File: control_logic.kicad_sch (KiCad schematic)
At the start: 33 parts, among them J18 USB_A_Stacked, J19 USB, J20 CTRL:ATU_L, J21 CTRL:FILT_H, J22 CTRL:FILT_L, J23 CTRL:ATU_H, U12 CM119B, U13 TUSB4041I, U14 BlackPill_STLINK, Y1 24Mhz

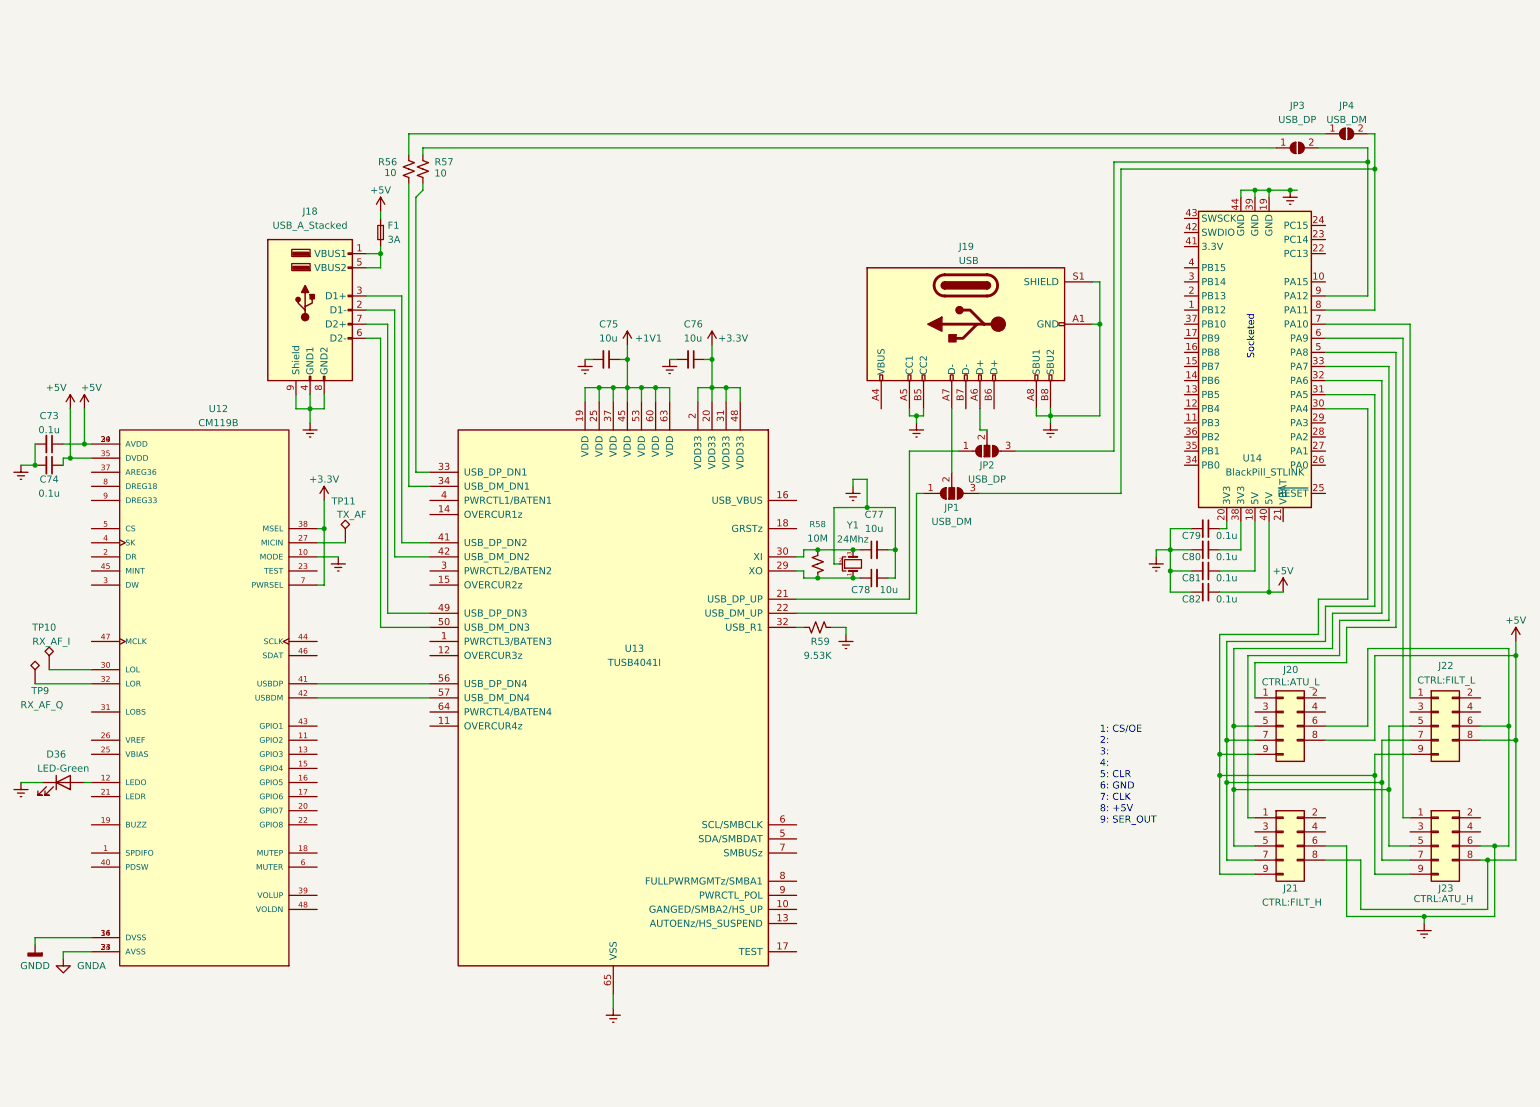
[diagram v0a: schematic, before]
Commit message: Replaced 74hc596 parts with mcp23017 and mcp23008 parts to simplify routing and reduce external parts count.
Added interface connectors for eventualy VHF (6m/2m/1.25m) RF path board.

Attempted to create some sort of documentations...
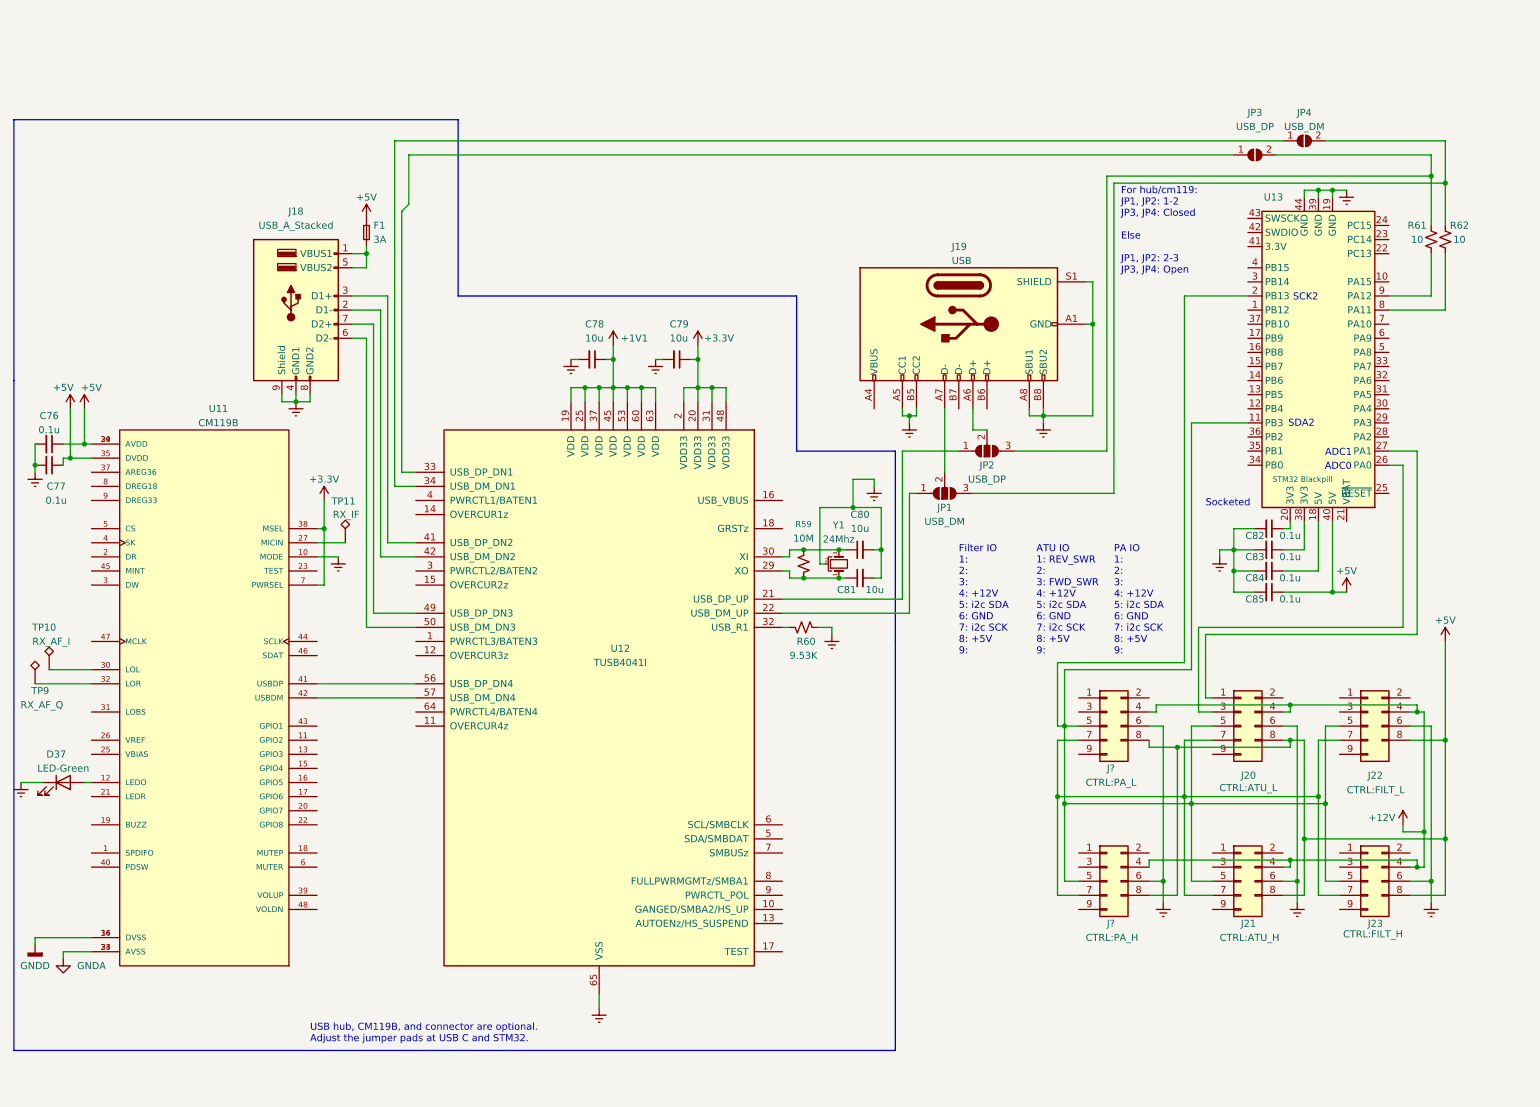
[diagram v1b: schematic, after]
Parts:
- removed R56, R57: 10, symbol Device:R_Small_US
- added J?: CTRL:PA_H, symbol Connector_Generic:Conn_2Rows-09Pins
- added J?: CTRL:PA_L, symbol Connector_Generic:Conn_2Rows-09Pins
- added R61, R62: 10, symbol Device:R_Small_US
- J21: value CTRL:FILT_H -> CTRL:ATU_H
- J23: value CTRL:ATU_H -> CTRL:FILT_H
- TP11: value TX_AF -> RX_IF
- U13: renamed from U14; value BlackPill_STLINK -> STM32 Blackpill
- renumbered C73 to C76, C74 to C77, C75 to C78, C76 to C79, C77 to C80, C78 to C81, C79 to C82, C80 to C83, C81 to C84, C82 to C85, D36 to D37, R58 to R59, R59 to R60, U12 to U11, U13 to U12
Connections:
- net +5V: now also J?.8 (Pin_8), J?.8 (Pin_8)
- net Earth: now also J?.6 (Pin_6), J?.6 (Pin_6)
- net at J21.1 (Pin_1): no longer U13.33 (PA7)
- net +12V: now reaches J21.4 (Pin_4)
- net +12V: now also J20.4 (Pin_4), J22.4 (Pin_4), J23.4 (Pin_4), J?.4 (Pin_4), J?.4 (Pin_4)
- net at J20.5 (Pin_5), J21.5 (Pin_5), J22.5 (Pin_5)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: now also U13.11 (PB3), U13.2 (PB13), J?.5 (Pin_5), J?.5 (Pin_5); no longer U13.32 (PA6)
- net at J20.7 (Pin_7), J21.7 (Pin_7), J22.7 (Pin_7)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: now also J?.7 (Pin_7), J?.7 (Pin_7); no longer U13.31 (PA5)
- net at U12.33 (USB_DP_DN1): now also JP3.1 (A)
- net at U12.34 (USB_DM_DN1): now also JP4.1 (A)
- net at J23.1 (Pin_1): no longer U13.6 (PA9)
- net at JP2.3 (B), JP3.2 (B): now also R61.2; no longer U13.9 (PA12)
- net at J20.1 (Pin_1): now also U13.27 (PA1); no longer U13.5 (PA8)
- net at J20.3 (Pin_3): now also U13.26 (PA0)
- net at JP1.3 (B), JP4.2 (B): now also R62.2; no longer U13.8 (PA11)
- net at J22.1 (Pin_1): no longer U13.7 (PA10)
- new net: R61.1, U13.9 (PA12)
- new net: R62.1, U13.8 (PA11)
- now unconnected: J20.9 (Pin_9), J21.9 (Pin_9), J22.9 (Pin_9), J23.9 (Pin_9), U13.30 (PA4)
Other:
- note added: "ADC0"
- note added: "ADC1"
- note added: "ATU IO 1: REV_SWR 2: 3: FWD_SWR 4: +12V 5: i2c SDA 6: GND 7: i2c SCK 8: +5V 9:"
- note added: "Filter IO 1: 2: 3: 4: +12V 5: i2c SDA 6: GND 7: i2c SCK 8: +5V 9:"
- note added: "For hub/cm119: JP1, JP2: 1-2 JP3, JP4: Closed Else JP1, JP2: 2-3 JP3, JP4: Open"
- note added: "PA IO 1: 2: 3: 4: +12V 5: i2c SDA 6: GND 7: i2c SCK 8: +5V 9:"
- note added: "SCK2"
- note added: "SDA2"
- note added: "USB hub, CM119B, and connector are optional. Adjust the jumper pads at USB C and STM32."
- note removed: "1: CS/OE 2: 3: 4: 5: CLR 6: GND 7: CLK 8: +5V 9: SER_OUT"
- moved on the sheet: C78, C79, C80, C81, C82, C83, C84, C85, F1, J18, J19, J20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

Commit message: cleanup of schematic and some initial firmware works...
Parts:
- removed C76, C77: 0.1u, Capacitor_THT:C_Disc_D4.7mm_W2.5mm_P5.00mm, symbol Device:C_Small
- removed D37: LED-Green, LED_SMD:LED_PLCC_2835_Handsoldering, symbol Device:LED
- removed J22: CTRL:FILT_L, symbol Connector_Generic:Conn_2Rows-09Pins
- removed J23: CTRL:FILT_H, symbol Connector_Generic:Conn_2Rows-09Pins
- removed JP3: USB_DP, symbol Jumper:SolderJumper_2_Open
- removed JP4: USB_DM, symbol Jumper:SolderJumper_2_Open
- removed TP10: RX_AF_I, symbol Connector:TestPoint_Alt
- removed TP11: RX_IF, symbol Connector:TestPoint_Alt
- removed TP9: RX_AF_Q, symbol Connector:TestPoint_Alt
- removed U11: CM119B, Package_QFP:TQFP-48_7x7mm_P0.5mm, symbol CM119B:CM119B
- added J24: CTRL:FILT_L, symbol Connector_Generic:Conn_2Rows-09Pins
- added J25: CTRL:FILT_H, symbol Connector_Generic:Conn_2Rows-09Pins
- added JP3: USB_DM, symbol Jumper:SolderJumper_3_Open
- added JP4: USB_DP, symbol Jumper:SolderJumper_3_Open
- C84: renamed from C80; value 10u -> 18p
- C85: renamed from C81; value 10u -> 18p
- gave numbers to parts that had none: 2
- renumbered C78 to C82, C79 to C83, C82 to C86, C83 to C87, C84 to C88, C85 to C89, J18 to J20, J19 to J21, J20 to J26, J21 to J27, R59 to R62, R60 to R63, R61 to R64, R62 to R65, U12 to U10, U13 to U11
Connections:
- net +12V: now also J24.4 (Pin_4), J25.4 (Pin_4)
- net +5V: now also J24.8 (Pin_8), J25.8 (Pin_8)
- net Earth: now also J24.6 (Pin_6), J25.6 (Pin_6)
- net at J27.1 (Pin_1): now also U11.27 (PA1)
- net at J27.2 (Pin_2): now also U11.31 (PA5)
- net at J27.3 (Pin_3): now also U11.26 (PA0)
- net at J23.5 (Pin_5), J27.5 (Pin_5), U11.11 (PB3): now also J25.5 (Pin_5); no longer J22.5 (Pin_5), J26.5 (Pin_5), U11.2 (PB13)
- net at J23.7 (Pin_7), J27.7 (Pin_7): now also U11.2 (PB13), J25.7 (Pin_7); no longer J22.7 (Pin_7), J26.7 (Pin_7)
- net at U10.21 (USB_DP_UP): now also JP4.1 (A); no longer JP2.1 (A)
- net at U10.22 (USB_DM_UP): now also JP3.1 (A); no longer JP1.1 (A)
- net at U10.33 (USB_DP_DN1): now also JP2.2 (C)
- net at U10.34 (USB_DM_DN1): now also JP1.2 (C)
- net at U10.41 (USB_DP_DN2): no longer J20.3 (D1+)
- net at U10.42 (USB_DM_DN2): no longer J20.2 (D1-)
- net at U10.49 (USB_DP_DN3): now also J20.3 (D1+); no longer J20.7 (D2+)
- net at U10.50 (USB_DM_DN3): now also J20.2 (D1-); no longer J20.6 (D2-)
- net at U10.56 (USB_DP_DN4): now also J20.7 (D2+)
- net at U10.57 (USB_DM_DN4): now also J20.6 (D2-)
- net at J21.A6 (D+): now also JP4.2 (C); no longer JP2.2 (C)
- net at R64.2: now also JP2.1 (A); no longer JP2.3 (B)
- net at J26.1 (Pin_1): now also U11.29 (PA3); no longer U11.27 (PA1)
- net at J26.2 (Pin_2): now also U11.30 (PA4)
- net at J26.3 (Pin_3): now also U11.28 (PA2); no longer U11.26 (PA0)
- net at J21.A7 (D-): now also JP3.2 (C); no longer JP1.2 (C)
- net at JP1.3 (B): now also JP3.3 (B); no longer R65.2
- net at J23.2 (Pin_2): now also U11.33 (PA7)
- net at J22.2 (Pin_2): now also U11.32 (PA6)
- net at U11.14 (PB6): now also J22.7 (Pin_7), J26.7 (Pin_7), J24.7 (Pin_7)
- net at U11.15 (PB7): now also J22.5 (Pin_5), J26.5 (Pin_5), J24.5 (Pin_5)
- new net: JP2.3 (B), JP4.3 (B)
- new net: JP1.1 (A), R65.2
- no-connect marks 0 -> 59
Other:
- note added: "ADC2"
- note added: "ADC3"
- note added: "ADC4"
- note added: "ADC5"
- note added: "ADC6"
- note added: "ADC7"
- note added: "ATU IO 1: REV_SWR 3: FWD_SWR 4: +12V 5: i2c SDA 6: GND 7: i2c SCK 8: +5V"
- note added: "Filter IO 4: +12V 5: i2c SDA 6: GND 7: i2c SCK 8: +5V"
- note added: "Hub/cm119: 1-2 Else: 2-3"
- note added: "PA IO 4: +12V 5: i2c SDA 6: GND 7: i2c SCK 8: +5V"
- note added: "SCK1"
- note added: "SDA1"
- note added: "THERMAL 1: Thermistor 1 2: Thermistor 2 3: Thermistor 3 4: NC 5: Thermistor 4 6: +5V 7: GND"
- note removed: "ATU IO 1: REV_SWR 2: 3: FWD_SWR 4: +12V 5: i2c SDA 6: GND 7: i2c SCK 8: +5V 9:"
- note removed: "Filter IO 1: 2: 3: 4: +12V 5: i2c SDA 6: GND 7: i2c SCK 8: +5V 9:"
- note removed: "For hub/cm119: JP1, JP2: 1-2 JP3, JP4: Closed Else JP1, JP2: 2-3 JP3, JP4: Open"
- note removed: "PA IO 1: 2: 3: 4: +12V 5: i2c SDA 6: GND 7: i2c SCK 8: +5V 9:"
- moved on the sheet: C82, C83, C84, C85, C86, C87, C88, C89, F1, J20, J21, J22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

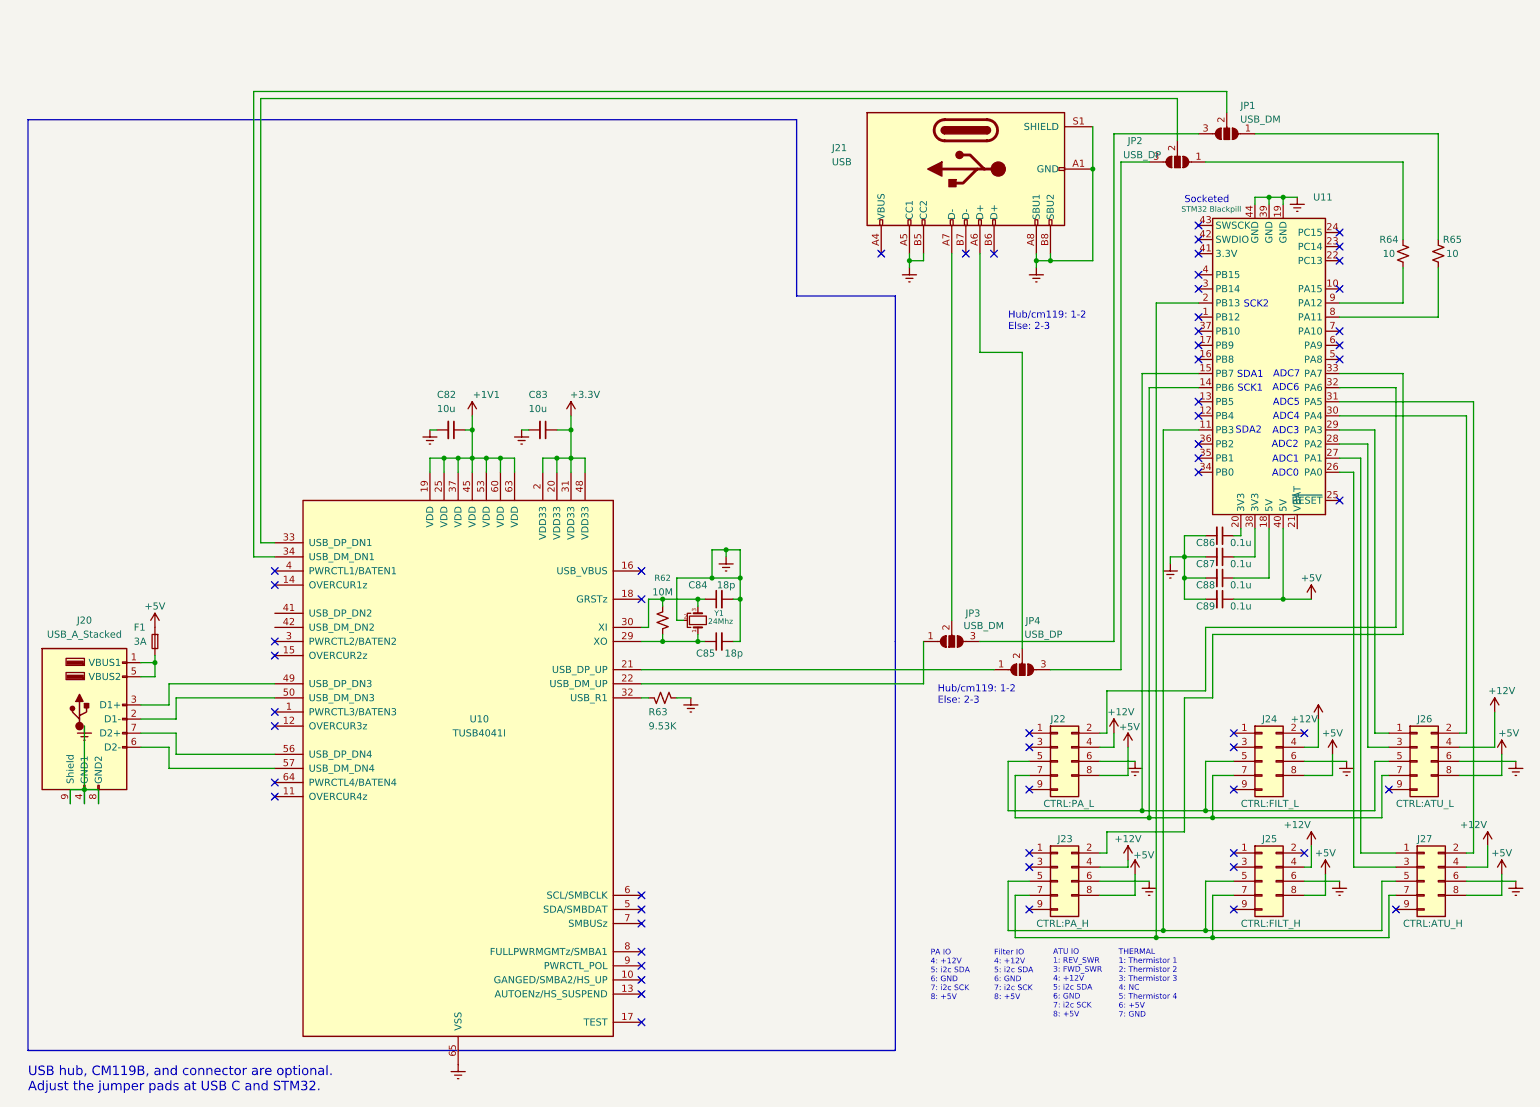
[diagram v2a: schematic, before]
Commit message: cleanup and start of introduction of www code
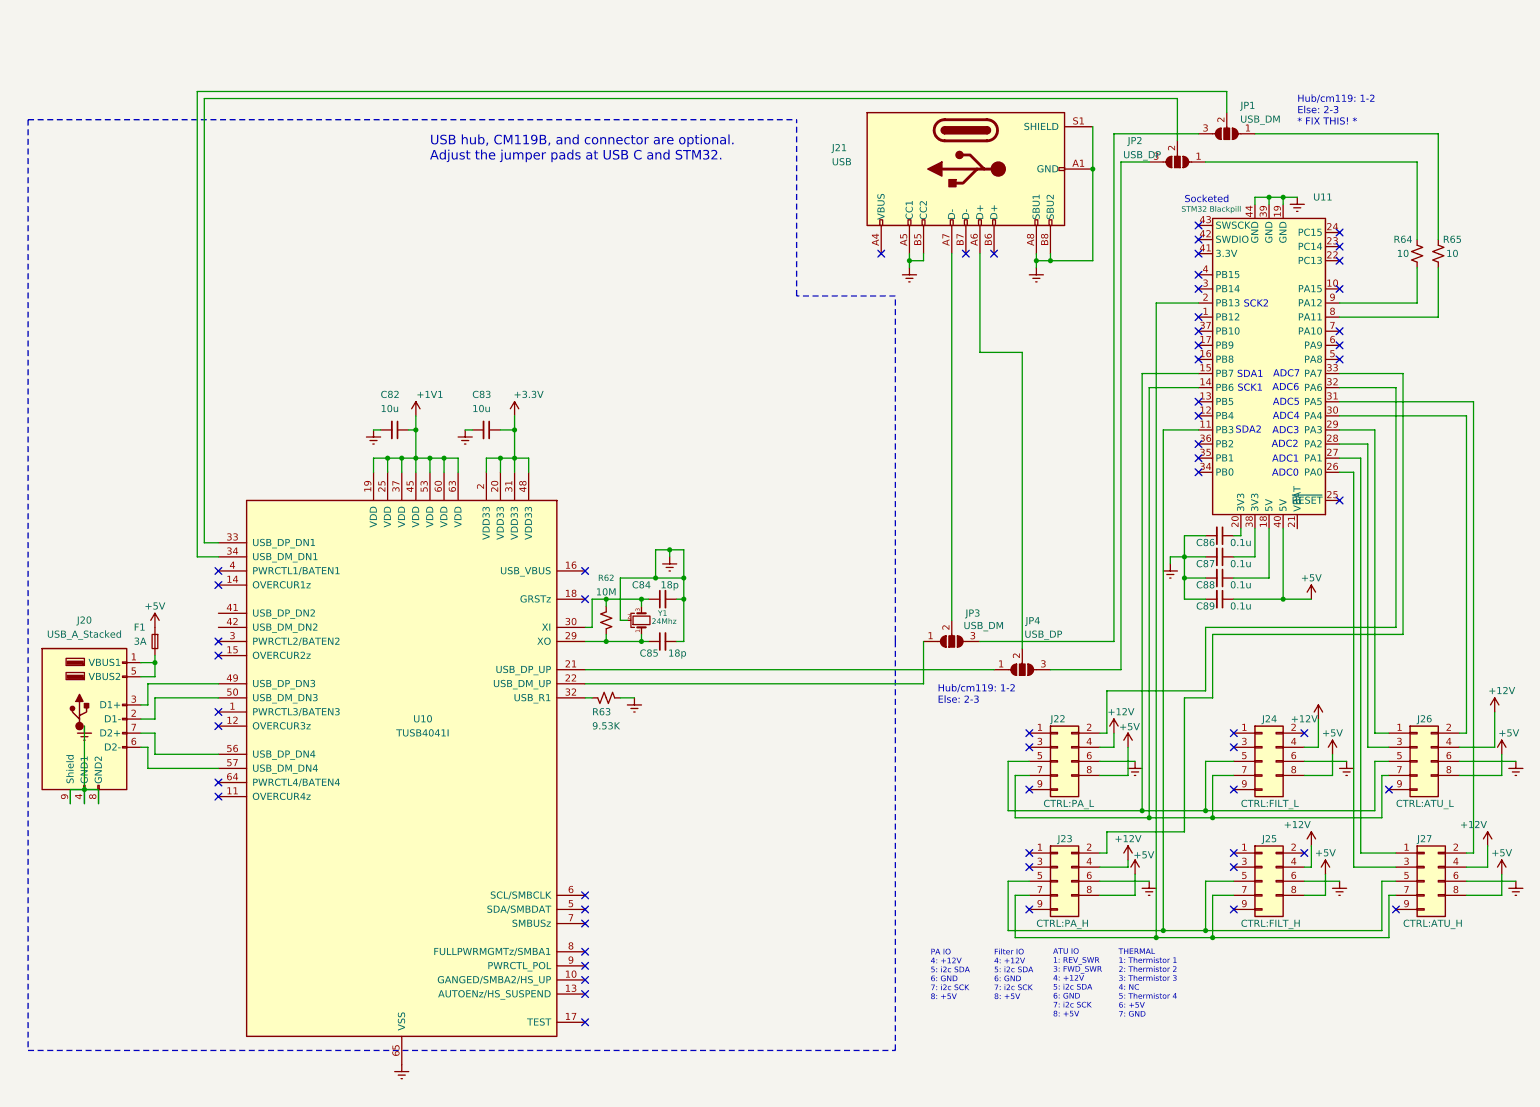
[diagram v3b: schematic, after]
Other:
- note added: "Hub/cm119: 1-2 Else: 2-3 * FIX THIS! *"
- moved on the sheet: C82, C83, C84, C85, R62, R63, R64, U10, Y1
